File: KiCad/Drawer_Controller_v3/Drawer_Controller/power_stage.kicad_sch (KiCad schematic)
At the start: 22 parts, among them U10 AMS1117-3.3, U11 LMR33630ADDAR

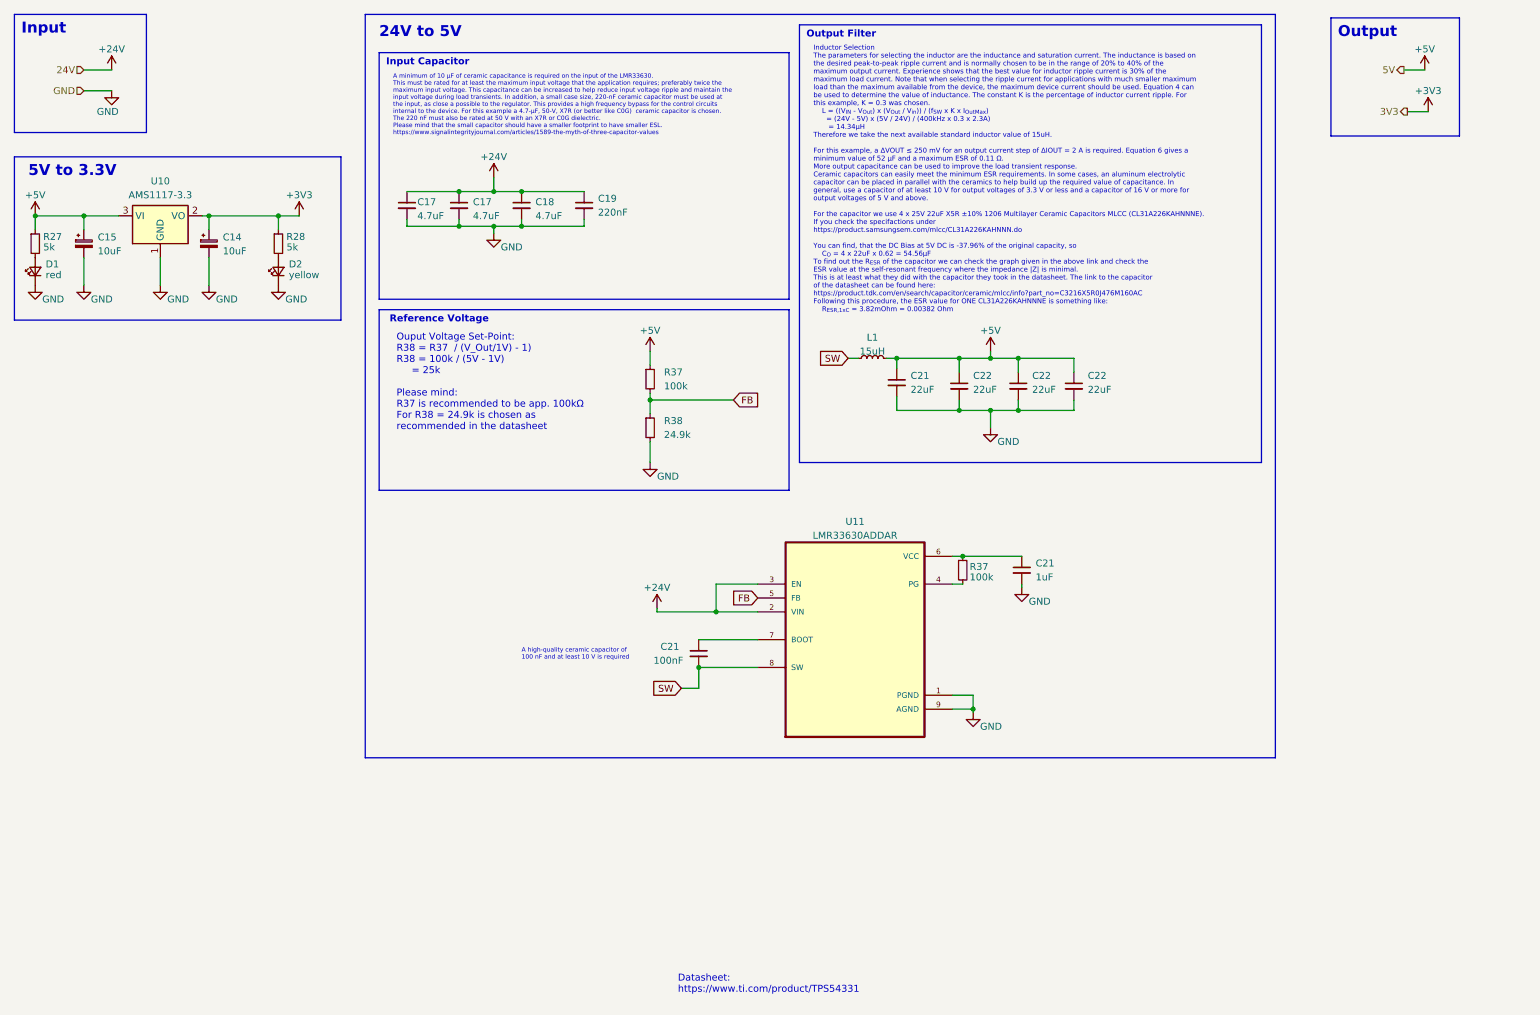
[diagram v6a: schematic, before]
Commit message: Fixing some ERC errors and warnings
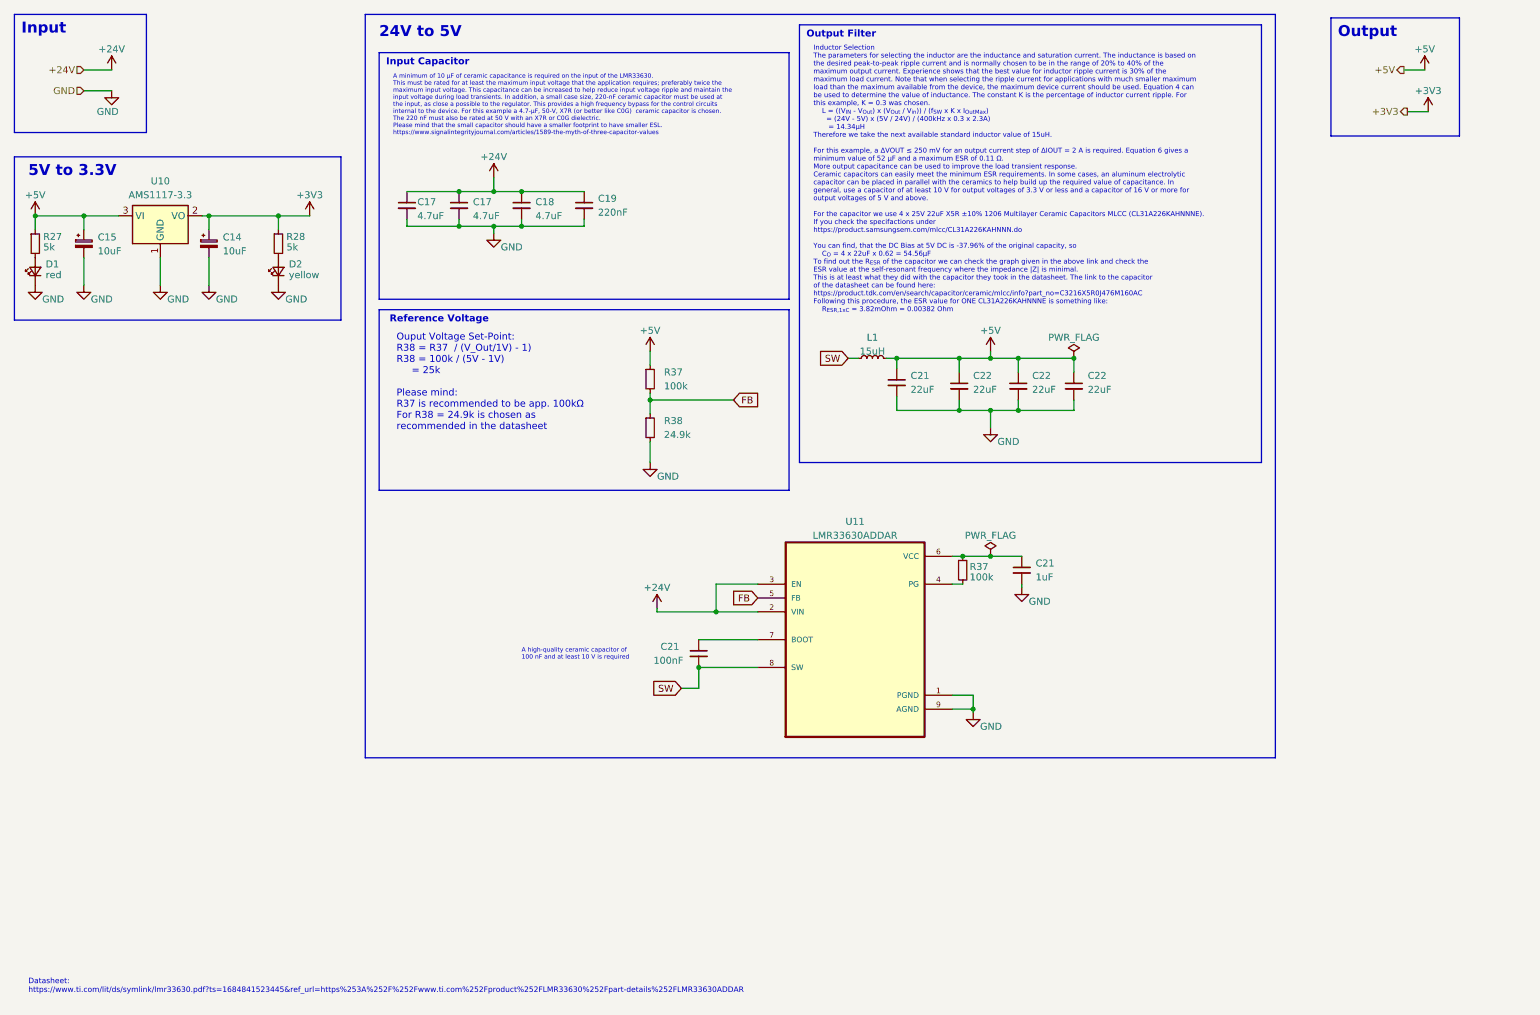
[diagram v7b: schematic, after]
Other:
- note added: "Datasheet: https://www.ti.com/lit/ds/symlink/lmr33630.pdf?ts=1684841523445&ref_url=https%253A%252F%252Fwww.ti.com%252Fproduct%252FLMR33630%252Fpart-details%252FLMR33630ADDAR"
- note removed: "Datasheet: https://www.ti.com/product/TPS54331"
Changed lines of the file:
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@@
   (junction (at 188.595 114.3) (diameter 0) (color 0 0 0 0)
   )
+  (junction (at 193.675 114.3) (diameter 0) (color 0 0 0 0)
+  )
   (junction (at 107.95 53.975) (diameter 0) (color 0 0 0 0)
   )
@@
   (junction (at 63.5 52.07) (diameter 0) (color 0 0 0 0)
   )
+  (junction (at 208.915 78.105) (diameter 0) (color 0 0 0 0)
+  )
   (junction (at 102.87 53.975) (diameter 0) (color 0 0 0 0)
   )
@@
     (stroke (width 0) (type default))
   )
+  (wire (pts (xy 193.675 114.3) (xy 199.39 114.3))
+    (stroke (width 0) (type default))
+  )
   (wire (pts (xy 187.96 78.105) (xy 193.675 78.105))
     (stroke (width 0) (type default))
@@
     (stroke (width 0) (type default))
   )
+  (wire (pts (xy 50.8 52.07) (xy 63.5 52.07))
+    (stroke (width 0) (type default))
+  )
   (wire (pts (xy 27.94 52.07) (xy 34.29 52.07))
     (stroke (width 0) (type default))
@@
     (stroke (width 0) (type default))
   )
-  (wire (pts (xy 50.8 52.07) (xy 63.5 52.07))
-    (stroke (width 0) (type default))
-  )
   (wire (pts (xy 193.675 76.835) (xy 193.675 78.105))
     (stroke (width 0) (type default))
@@
     (stroke (width 0) (type default))
   )
-  (wire (pts (xy 188.595 114.3) (xy 199.39 114.3))
+  (wire (pts (xy 188.595 114.3) (xy 193.675 114.3))
     (stroke (width 0) (type default))
   )
@@
     (stroke (width 0) (type default))
   )
-  (wire (pts (xy 63.5 52.07) (xy 67.31 52.07))
+  (wire (pts (xy 63.5 52.07) (xy 69.215 52.07))
     (stroke (width 0) (type default))
   )
@@
     (effects (font (size 2 2) (thickness 0.4) bold) (justify left bottom))
   )
-  (text "Datasheet:\nhttps://www.ti.com/product/TPS54331" (at 136.525 194.31 0)
-    (effects (font (size 1.27 1.27)) (justify left bottom))
+  (text "Datasheet:\nhttps://www.ti.com/lit/ds/symlink/lmr33630.pdf?ts=1684841523445&ref_url=https%253A%252F%252Fwww.ti.com%252Fproduct%252FLMR33630%252Fpart-details%252FLMR33630ADDAR"
+    (at 17.78 194.31 0)
+    (effects (font (size 1 1)) (justify left bottom))
   )
   (text "Output Filter" (at 160.02 19.685 0)
@@
     (effects (font (size 1.27 1.27)) (justify right))
   )
-  (hierarchical_label "3V3" (shape output) (at 269.875 33.02 180) (fields_autoplaced)
+  (hierarchical_label "+3V3" (shape output) (at 269.875 33.02 180) (fields_autoplaced)
     (effects (font (size 1.27 1.27)) (justify right))
   )
-  (hierarchical_label "5V" (shape output) (at 269.24 25.4 180) (fields_autoplaced)
+  (hierarchical_label "+5V" (shape output) (at 269.24 25.4 180) (fields_autoplaced)
     (effects (font (size 1.27 1.27)) (justify right))
   )
-  (hierarchical_label "24V" (shape input) (at 27.94 25.4 180) (fields_autoplaced)
+  (hierarchical_label "+24V" (shape input) (at 27.94 25.4 180) (fields_autoplaced)
     (effects (font (size 1.27 1.27)) (justify right))
   )
@@
     )
   )
-  (symbol (lib_id "power:+3V3") (at 67.31 52.07 0) (unit 1)
+  (symbol (lib_id "power:+3V3") (at 69.215 52.07 0) (unit 1)
     (in_bom yes) (on_board yes) (dnp no) (fields_autoplaced)
-    (property "Reference" "#PWR065" (at 67.31 55.88 0)
-      (effects (font (size 1.27 1.27)) hide)
-    )
-    (property "Value" "+3V3" (at 67.31 48.26 0)
-      (effects (font (size 1.27 1.27)))
-    )
-    (property "Footprint" "" (at 67.31 52.07 0)
-      (effects (font (size 1.27 1.27)) hide)
-    )
-    (property "Datasheet" "" (at 67.31 52.07 0)
+    (property "Reference" "#PWR065" (at 69.215 55.88 0)
+      (effects (font (size 1.27 1.27)) hide)
+    )
+    (property "Value" "+3V3" (at 69.215 48.26 0)
+      (effects (font (size 1.27 1.27)))
+    )
+    (property "Footprint" "" (at 69.215 52.07 0)
+      (effects (font (size 1.27 1.27)) hide)
+    )
+    (property "Datasheet" "" (at 69.215 52.07 0)
       (effects (font (size 1.27 1.27)) hide)
     )
@@
     )
   )
+  (symbol (lib_id "power:PWR_FLAG") (at 193.675 114.3 0) (unit 1)
+    (in_bom yes) (on_board yes) (dnp no) (fields_autoplaced)
+    (property "Reference" "#FLG07" (at 193.675 112.395 0)
+      (effects (font (size 1.27 1.27)) hide)
+    )
+    (property "Value" "PWR_FLAG" (at 193.675 110.49 0)
+      (effects (font (size 1.27 1.27)))
+    )
+    (property "Footprint" "" (at 193.675 114.3 0)
+      (effects (font (size 1.27 1.27)) hide)
+    )
+    (property "Datasheet" "~" (at 193.675 114.3 0)
+      (effects (font (size 1.27 1.27)) hide)
+    )
+    (pin "1")
+    (instances
+      (project "Drawer_Controller"
+        (path "/9538e4ed-27e6-4c37-b989-9859dc0d49e8/8d969422-65ba-4eec-9081-e3062cead741"
+          (reference "#FLG07") (unit 1)
+        )
+      )
+    )
+  )
   (symbol (lib_id "Device:R_Small") (at 131.445 81.915 0) (unit 1)
     (in_bom yes) (on_board yes) (dnp no)
@@
         )
       )
+    )
+  )
+  (symbol (lib_id "power:PWR_FLAG") (at 208.915 78.105 0) (unit 1)
+    (in_bom yes) (on_board yes) (dnp no) (fields_autoplaced)
+    (property "Reference" "#FLG01" (at 208.915 76.2 0)
+      (effects (font (size 1.27 1.27)) hide)
+    )
+    (property "Value" "PWR_FLAG" (at 208.915 74.295 0)
+      (effects (font (size 1.27 1.27)))
+    )
+    (property "Footprint" "" (at 208.915 78.105 0)
+      (effects (font (size 1.27 1.27)) hide)
+    )
+    (property "Datasheet" "~" (at 208.915 78.105 0)
+      (effects (font (size 1.27 1.27)) hide)
+    )
+    (pin "1")
+    (instances
+      (project "Drawer_Controller"
+        (path "/9538e4ed-27e6-4c37-b989-9859dc0d49e8/1e76985c-8d5c-4698-93c6-d17abaa8f3ee"
+          (reference "#FLG01") (unit 1)
+        )
+        (path "/9538e4ed-27e6-4c37-b989-9859dc0d49e8/116698a8-1d79-42ab-8e41-bc8a6feebb86"
+          (reference "#FLG02") (unit 1)
+        )
+        (path "/9538e4ed-27e6-4c37-b989-9859dc0d49e8"
+          (reference "#FLG01") (unit 1)
+        )
+        (path "/9538e4ed-27e6-4c37-b989-9859dc0d49e8/8d969422-65ba-4eec-9081-e3062cead741"
+          (reference "#FLG03") (unit 1)
+        )
+      )

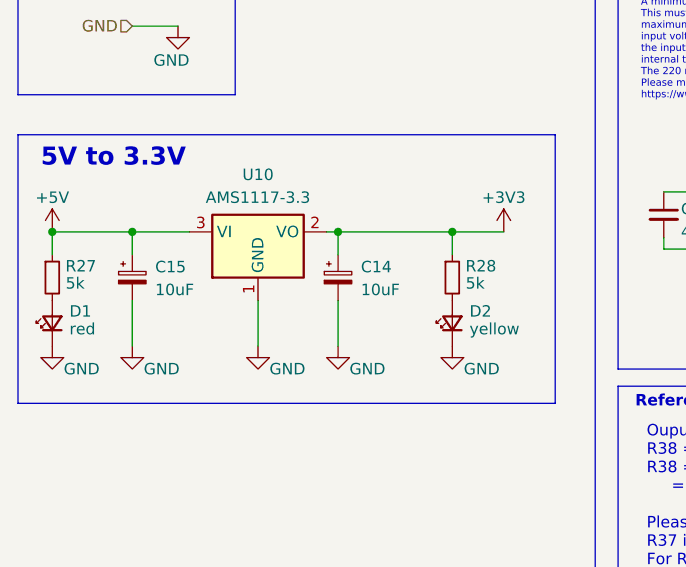
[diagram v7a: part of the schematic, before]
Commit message: Finished assigning all footprints
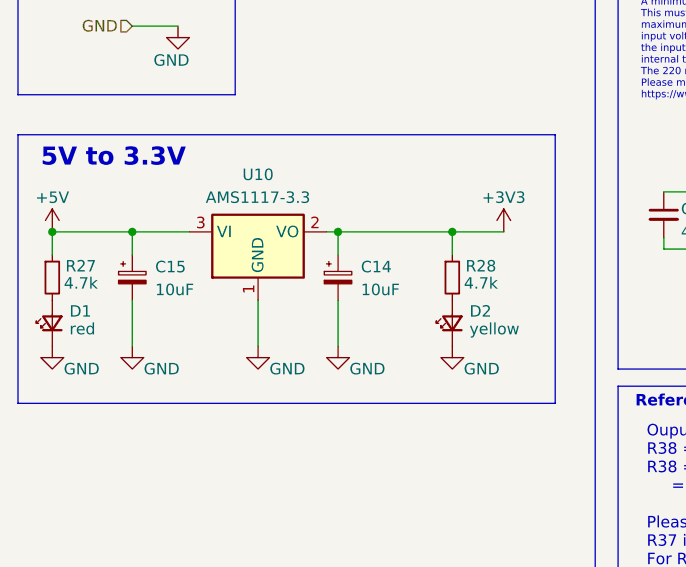
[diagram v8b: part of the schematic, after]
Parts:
- C14, C15, R37, R38: footprint (none) -> Capacitor_SMD:C_0603_1608Metric
- C17, C18, C21, C22: footprint (none) -> Capacitor_SMD:C_1206_3216Metric
- C19, C21: footprint (none) -> Capacitor_SMD:C_0805_2012Metric
- C21: footprint (none) -> Capacitor_SMD:C_0402_1005Metric
- D1: footprint LED_SMD:LED_0603_1608Metric_Pad1.05x0.95mm_HandSolder -> LED_SMD:LED_0603_1608Metric
- D2: footprint LED_SMD:LED_0603_1608Metric_Pad1.05x0.95mm_HandSolder -> LED_SMD:LED_0805_2012Metric
- L1: footprint (none) -> Robast_Footprints:SMDRI127-150MT
- R27, R28: value 5k -> 4.7k; footprint Resistor_SMD:R_0805_2012Metric_Pad1.20x1.40mm_HandSolder -> Capacitor_SMD:C_0603_1608Metric
- U11: footprint VREG_LM5017MR/NOPB -> Robast_Footprints:LMR33630ADDAR
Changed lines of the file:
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@@
       (effects (font (size 1.27 1.27)) (justify left))
     )
-    (property "Footprint" "" (at 27.94 57.15 0)
+    (property "Footprint" "Capacitor_SMD:C_0603_1608Metric" (at 27.94 57.15 0)
       (effects (font (size 1.27 1.27)) hide)
     )
@@
       (effects (font (size 1.27 1.27)) (justify left))
     )
-    (property "Footprint" "" (at 96.52 50.165 0)
+    (property "Footprint" "Capacitor_SMD:C_1206_3216Metric" (at 96.52 50.165 0)
       (effects (font (size 1.27 1.27)) hide)
     )
@@
       (effects (font (size 1.27 1.27)))
     )
-    (property "Footprint" "VREG_LM5017MR/NOPB" (at 168.91 129.54 0)
+    (property "Footprint" "Robast_Footprints:LMR33630ADDAR" (at 168.91 129.54 0)
       (effects (font (size 1.27 1.27)) (justify bottom) hide)
     )
@@
       (effects (font (size 1.27 1.27)) (justify left))
     )
-    (property "Footprint" "" (at 131.445 90.805 0)
+    (property "Footprint" "Capacitor_SMD:C_0603_1608Metric" (at 131.445 90.805 0)
       (effects (font (size 1.27 1.27)) hide)
     )
@@
       (effects (font (size 1.27 1.27)) (justify left))
     )
-    (property "Footprint" "" (at 140.335 132.08 0)
+    (property "Footprint" "Capacitor_SMD:C_0402_1005Metric" (at 140.335 132.08 0)
       (effects (font (size 1.27 1.27)) hide)
     )
@@
       (effects (font (size 1.27 1.27)) (justify left))
     )
-    (property "Footprint" "" (at 208.915 83.185 0)
+    (property "Footprint" "Capacitor_SMD:C_1206_3216Metric" (at 208.915 83.185 0)
       (effects (font (size 1.27 1.27)) hide)
     )
@@
       (effects (font (size 1.27 1.27)) (justify left))
     )
-    (property "Footprint" "" (at 176.53 82.55 0)
+    (property "Footprint" "Capacitor_SMD:C_1206_3216Metric" (at 176.53 82.55 0)
       (effects (font (size 1.27 1.27)) hide)
     )
@@
       (effects (font (size 1.27 1.27)) (justify left))
     )
-    (property "Footprint" "" (at 50.8 57.15 0)
+    (property "Footprint" "Capacitor_SMD:C_0603_1608Metric" (at 50.8 57.15 0)
       (effects (font (size 1.27 1.27)) hide)
     )
@@
       (effects (font (size 1.27 1.27)) (justify right))
     )
-    (property "Footprint" "LED_SMD:LED_0603_1608Metric_Pad1.05x0.95mm_HandSolder" (at 19.05 62.23 90)
+    (property "Footprint" "LED_SMD:LED_0603_1608Metric" (at 19.05 62.23 90)
       (effects (font (size 1.27 1.27)) hide)
     )
@@
       (effects (font (size 1.27 1.27)) (justify left))
     )
-    (property "Footprint" "" (at 107.95 50.165 0)
+    (property "Footprint" "Capacitor_SMD:C_1206_3216Metric" (at 107.95 50.165 0)
       (effects (font (size 1.27 1.27)) hide)
     )
@@
       (effects (font (size 1.27 1.27)) (justify left))
     )
-    (property "Footprint" "" (at 86.995 50.165 0)
+    (property "Footprint" "Capacitor_SMD:C_1206_3216Metric" (at 86.995 50.165 0)
       (effects (font (size 1.27 1.27)) hide)
     )
@@
       (effects (font (size 1.27 1.27)) (justify left))
     )
-    (property "Footprint" "" (at 131.445 81.915 0)
+    (property "Footprint" "Capacitor_SMD:C_0603_1608Metric" (at 131.445 81.915 0)
       (effects (font (size 1.27 1.27)) hide)
     )
@@
       (effects (font (size 1.27 1.27)) (justify left))
     )
-    (property "Footprint" "" (at 198.755 83.185 0)
+    (property "Footprint" "Capacitor_SMD:C_1206_3216Metric" (at 198.755 83.185 0)
       (effects (font (size 1.27 1.27)) hide)
     )
@@
       (effects (font (size 1.27 1.27)) (justify right))
     )
-    (property "Footprint" "LED_SMD:LED_0603_1608Metric_Pad1.05x0.95mm_HandSolder" (at 63.5 62.23 90)
+    (property "Footprint" "LED_SMD:LED_0805_2012Metric" (at 63.5 62.23 90)
       (effects (font (size 1.27 1.27)) hide)
     )
@@
       (effects (font (size 1.27 1.27)))
     )
-    (property "Value" "5k" (at 66.04 57.785 0)
-      (effects (font (size 1.27 1.27)))
-    )
-    (property "Footprint" "Resistor_SMD:R_0805_2012Metric_Pad1.20x1.40mm_HandSolder" (at 63.5 57.15 0)
+    (property "Value" "4.7k" (at 66.675 57.785 0)
+      (effects (font (size 1.27 1.27)))
+    )
+    (property "Footprint" "Capacitor_SMD:C_0603_1608Metric" (at 63.5 57.15 0)
       (effects (font (size 1.27 1.27)) hide)
     )
@@
       (effects (font (size 1.27 1.27)) (justify left))
     )
-    (property "Footprint" "" (at 199.39 116.84 0)
+    (property "Footprint" "Capacitor_SMD:C_0805_2012Metric" (at 199.39 116.84 0)
       (effects (font (size 1.27 1.27)) hide)
     )
@@
       (effects (font (size 1.27 1.27)) (justify left))
     )
-    (property "Footprint" "" (at 119.38 50.165 0)
+    (property "Footprint" "Capacitor_SMD:C_0805_2012Metric" (at 119.38 50.165 0)
       (effects (font (size 1.27 1.27)) hide)
     )
@@
       (effects (font (size 1.27 1.27)) (justify left))
     )
-    (property "Footprint" "" (at 188.595 116.84 0)
+    (property "Footprint" "Capacitor_SMD:C_0603_1608Metric" (at 188.595 116.84 0)
       (effects (font (size 1.27 1.27)) hide)
     )
@@
       (effects (font (size 1.27 1.27)) (justify left))
     )
-    (property "Footprint" "" (at 187.96 83.185 0)
+    (property "Footprint" "Capacitor_SMD:C_1206_3216Metric" (at 187.96 83.185 0)
       (effects (font (size 1.27 1.27)) hide)
     )
@@
       (effects (font (size 1.27 1.27)))
     )
-    (property "Footprint" "" (at 172.085 78.105 0)
+    (property "Footprint" "Robast_Footprints:SMDRI127-150MT" (at 172.085 78.105 0)
       (effects (font (size 1.27 1.27)) hide)
     )
@@
       (effects (font (size 1.27 1.27)))
     )
-    (property "Value" "5k" (at 21.59 57.785 0)
-      (effects (font (size 1.27 1.27)))
-    )
-    (property "Footprint" "Resistor_SMD:R_0805_2012Metric_Pad1.20x1.40mm_HandSolder" (at 19.05 57.15 0)
-      (effects (font (size 1.27 1.27)) hide)
-    )
+    (property "Value" "4.7k" (at 22.225 57.785 0)
+      (effects (font (size 1.27 1.27)))
+    )
+    (property "Footprint" "Capacitor_SMD:C_0603_1608Metric" (at 19.05 57.15 0)
+      (effects (font (size 1.27 1.27)) hide)
+    )
